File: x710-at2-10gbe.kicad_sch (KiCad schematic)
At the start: 18 parts, among them U1 EZX710AT2_S_LMR5

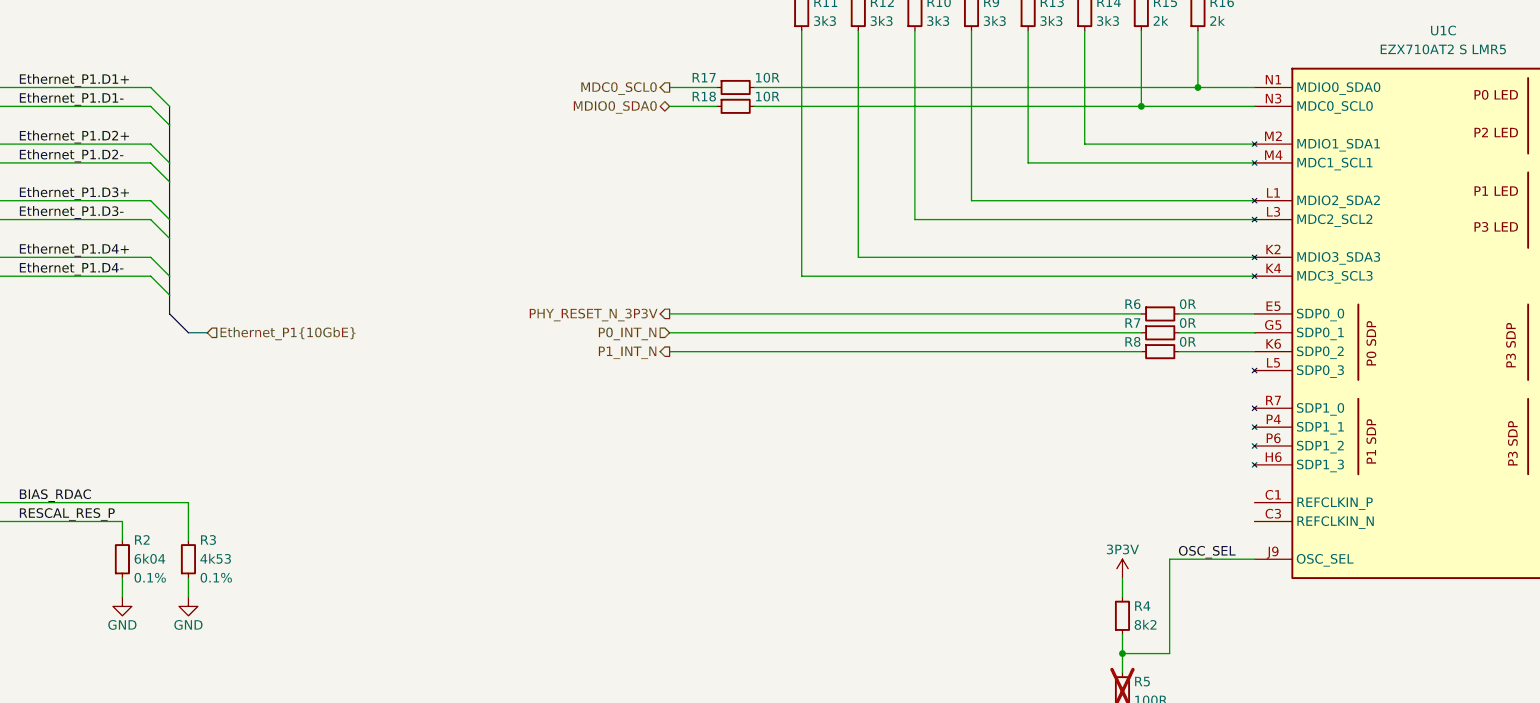
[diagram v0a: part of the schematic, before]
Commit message: [#80813] Add RJ45 connectors, add SMBus, FLASH SPI and misc
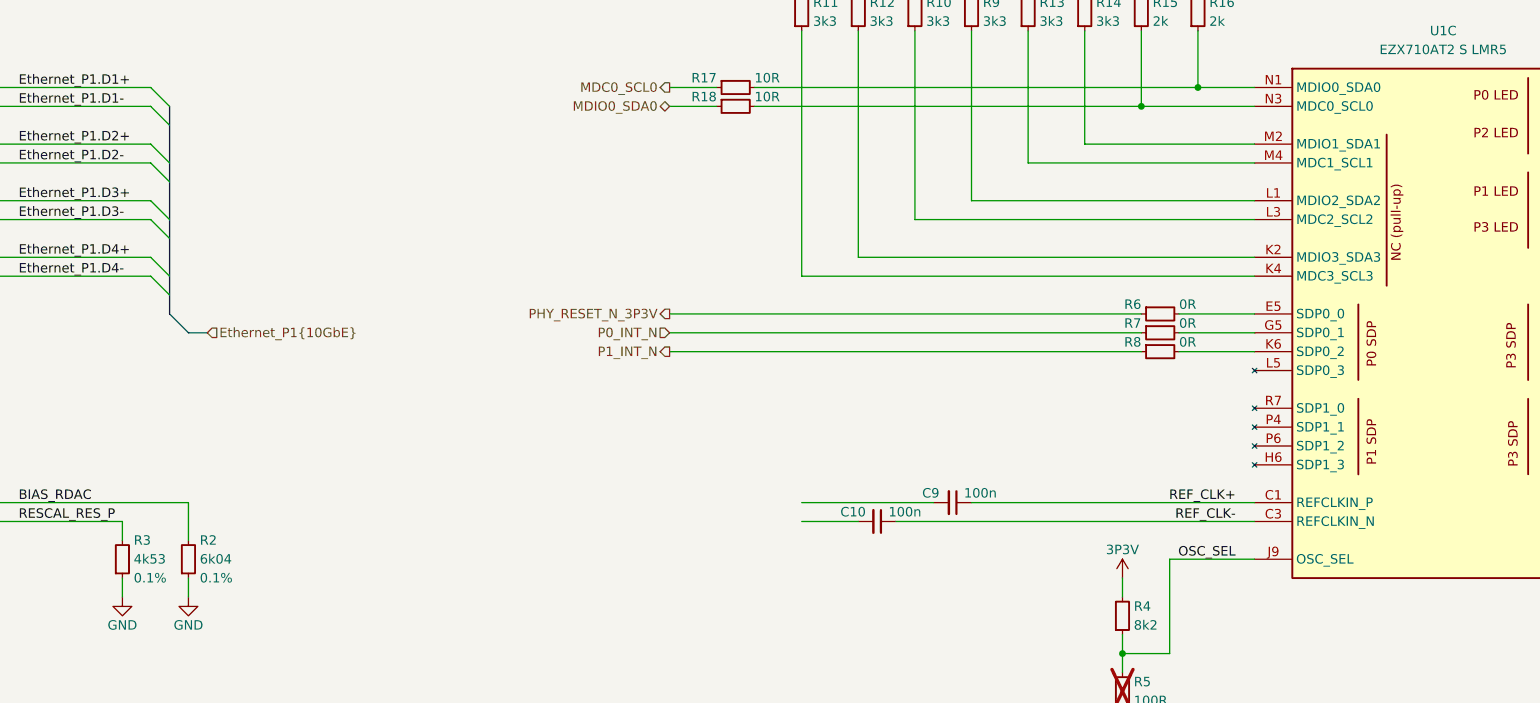
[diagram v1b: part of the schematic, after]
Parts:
- added C10, C9: C_100n_16V_X7R_0402, antmicro-footprints:C_0402_1005Metric, symbol antmicroCapacitors0402:C_100n_16V_X7R_0402
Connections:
- net BIAS_RDAC: now also R2.2; no longer R3.2
- net RESCAL_RES_P: now also R3.2; no longer R2.2
- net REF_CLK+: now reaches U1.C1 (REFCLKIN_P)
- net REF_CLK+: now also C9.1
- net REF_CLK-: now reaches U1.C3 (REFCLKIN_N)
- net REF_CLK-: now also C10.1
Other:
- moved on the sheet: R2, R3

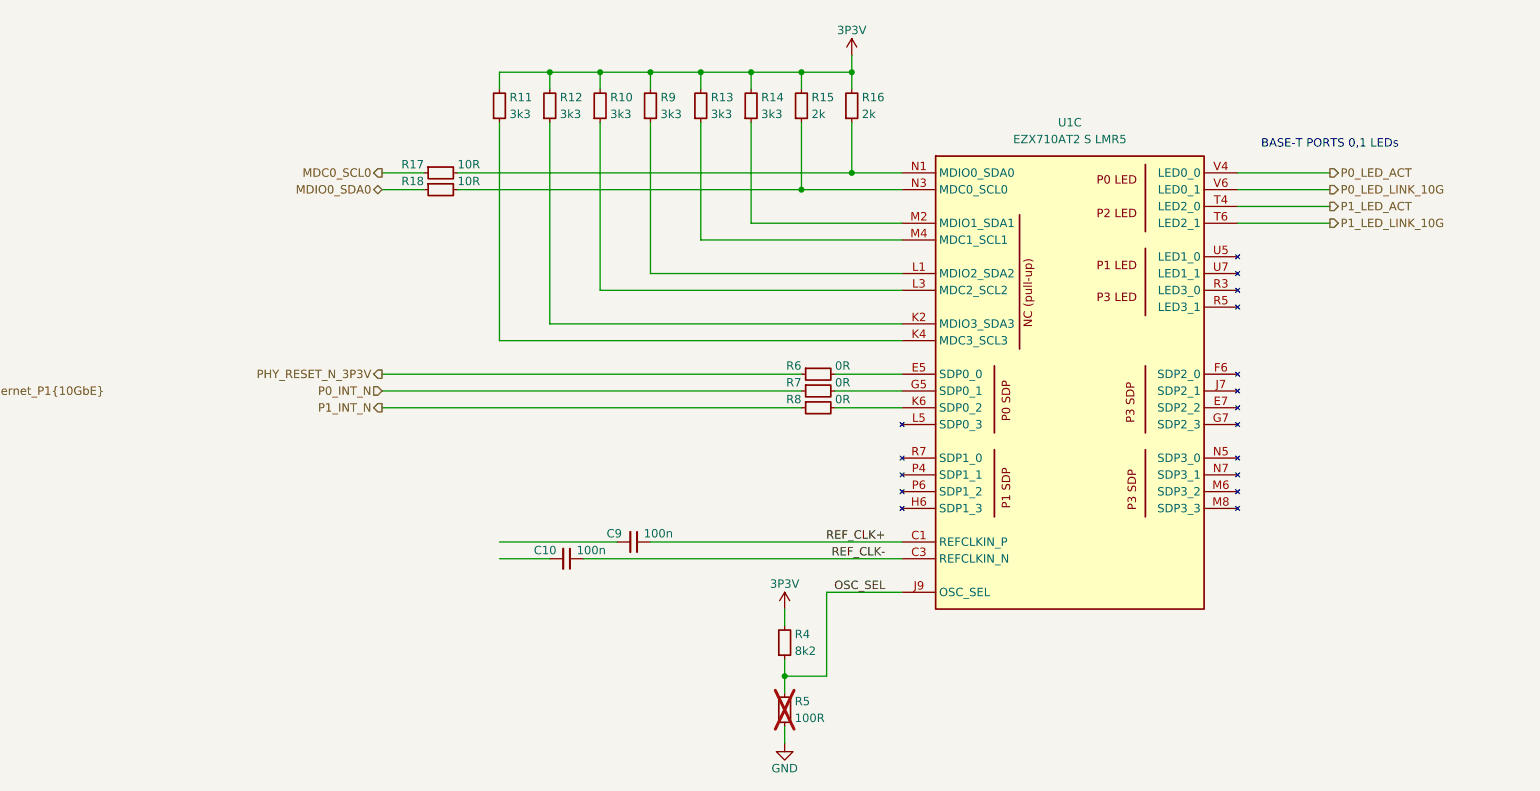
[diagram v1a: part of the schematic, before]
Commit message: [#80813] Add misc, improve schematic readability
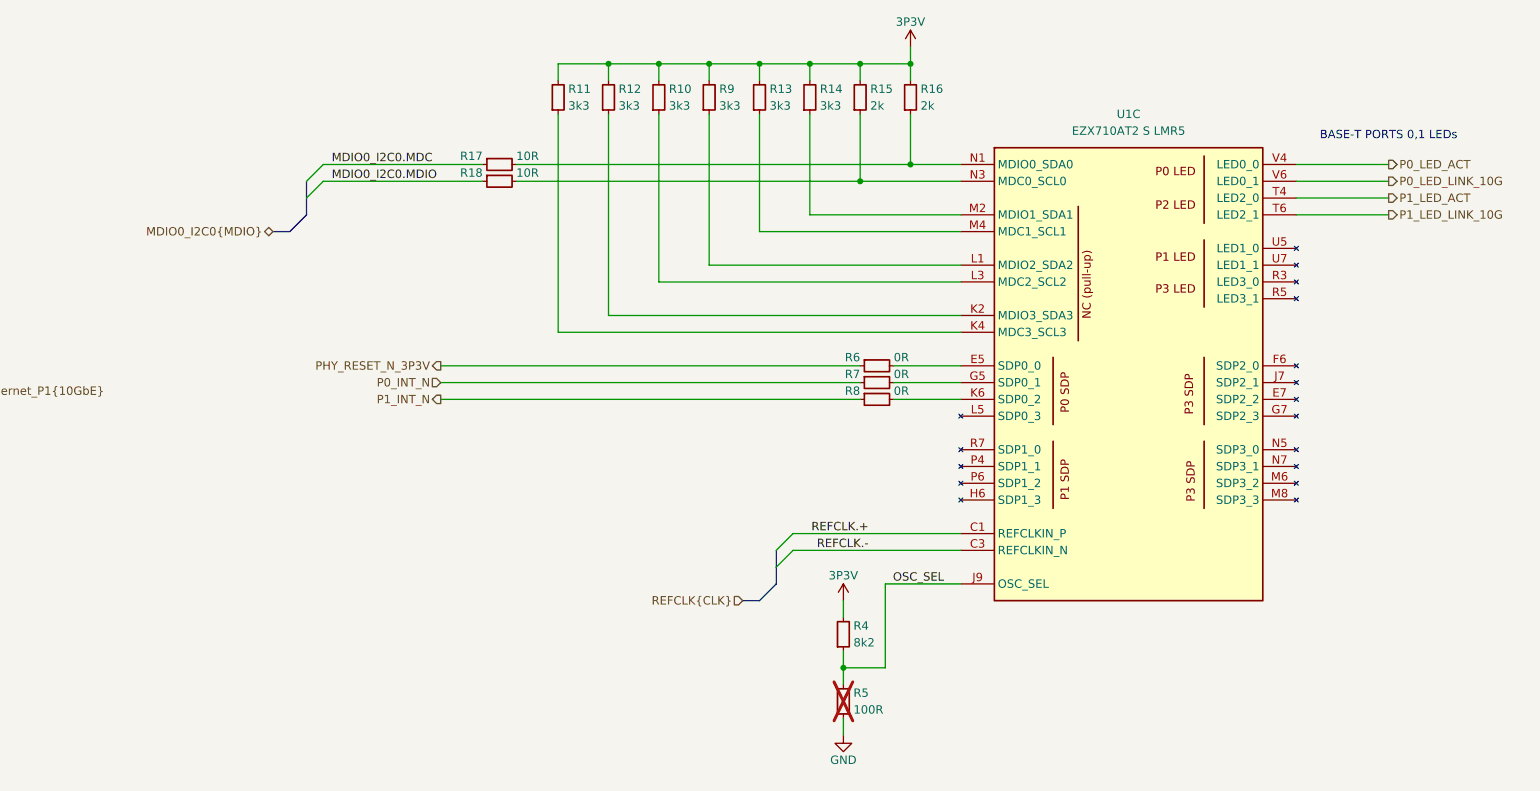
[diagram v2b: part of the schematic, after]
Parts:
- removed C10, C9: C_100n_16V_X7R_0402, antmicro-footprints:C_0402_1005Metric, symbol antmicroCapacitors0402:C_100n_16V_X7R_0402
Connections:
- net MDC0_SCL0 renamed MDIO0_I2C0.MDC
- net MDIO0_SDA0 renamed MDIO0_I2C0.MDIO
- net REF_CLK+ renamed REFCLK.+
- net REF_CLK- renamed REFCLK.-
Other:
- moved on the sheet: R10, R11, R12, R13, R14, R15, R16, R17, R18, R4, R5, R6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

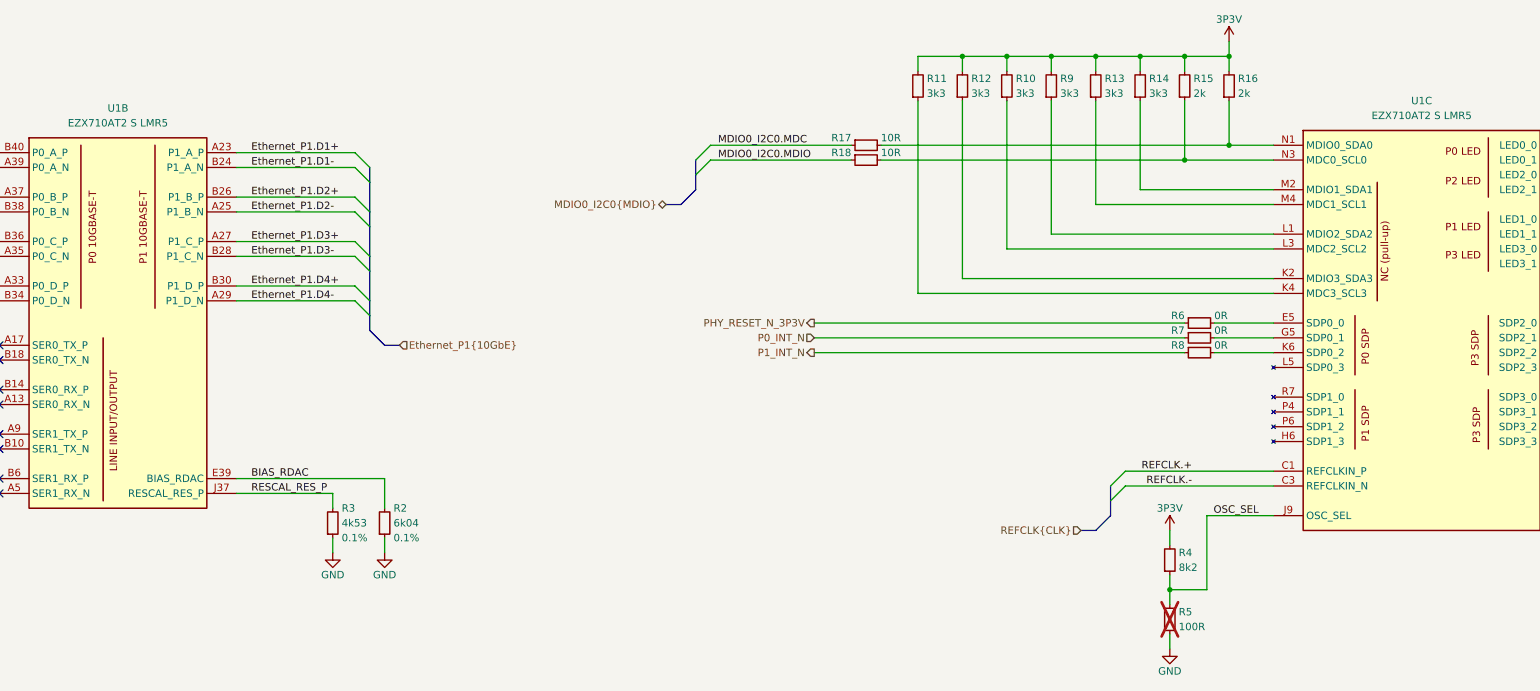
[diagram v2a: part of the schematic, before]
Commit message: [#80813] Change RJ45 connectors, reannotate schematics
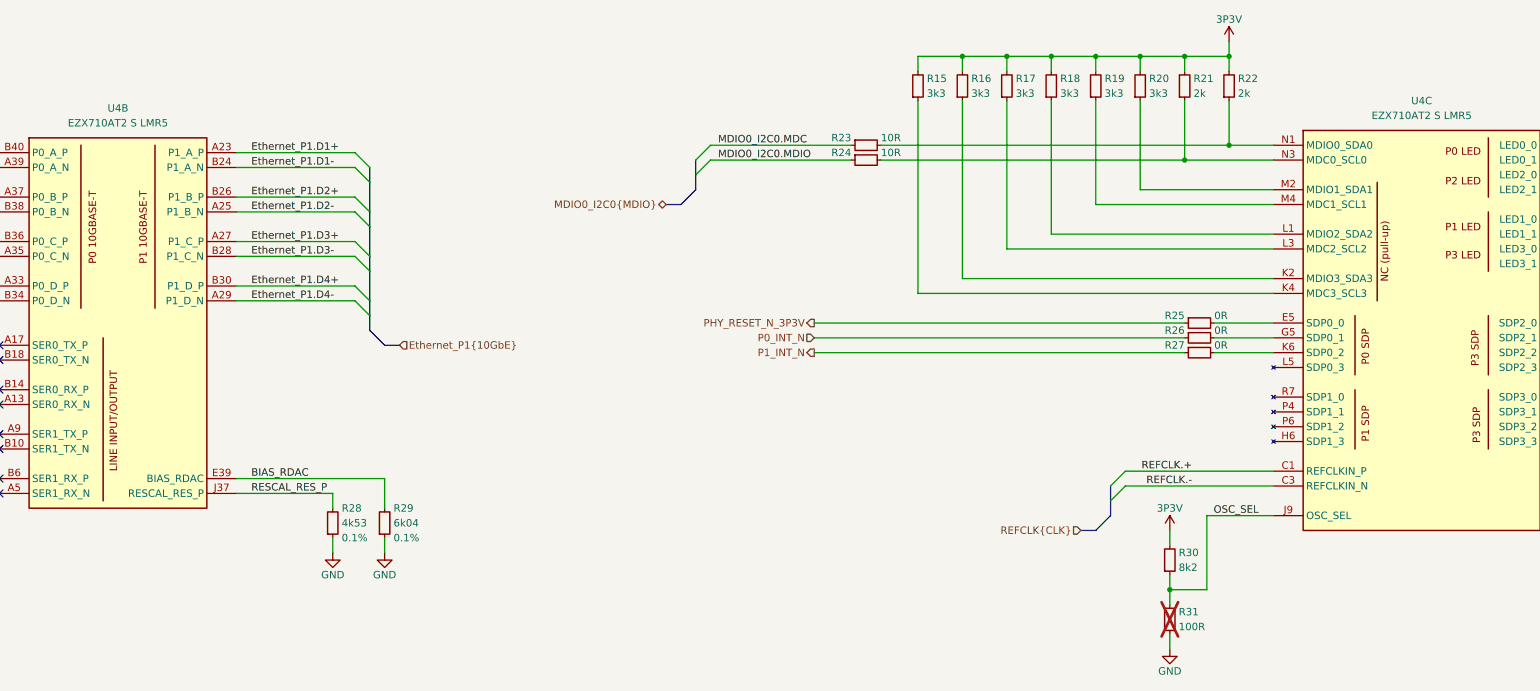
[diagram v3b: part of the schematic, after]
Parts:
- renumbered R11 to R15, R12 to R16, R10 to R17, R9 to R18, R13 to R19, R14 to R20, R15 to R21, R16 to R22, R17 to R23, R18 to R24, R6 to R25, R7 to R26, R8 to R27, R3 to R28, R2 to R29, R4 to R30, R5 to R31, U1 to U4
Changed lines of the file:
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@@
 		(on_board yes)
 		(dnp no)
-		(property "Reference" "#PWR02"
+		(property "Reference" "#PWR049"
 			(at 172.72 193.04 0)
 			(effects
@@
 			(project "10-gbe-expansion"
 				(path "/04bda987-e5eb-48b4-9e90-d8211dc11b39/46fcd652-659b-4e06-aa16-4947b5e55b68"
-					(reference "#PWR02")
+					(reference "#PWR049")
 					(unit 1)
 				)
@@
 		(on_board yes)
 		(dnp no)
-		(property "Reference" "R8"
+		(property "Reference" "R27"
 			(at 300.99 154.94 0)
 			(effects
@@
 			(project "10-gbe-expansion"
 				(path "/04bda987-e5eb-48b4-9e90-d8211dc11b39/46fcd652-659b-4e06-aa16-4947b5e55b68"
-					(reference "R8")
+					(reference "R27")
 					(unit 1)
 				)
@@
 		(on_board yes)
 		(dnp no)
-		(property "Reference" "R4"
+		(property "Reference" "R30"
 			(at 299.974 190.5 90)
 			(effects
@@
 			(project ""
 				(path "/04bda987-e5eb-48b4-9e90-d8211dc11b39/46fcd652-659b-4e06-aa16-4947b5e55b68"
-					(reference "R4")
+					(reference "R30")
 					(unit 1)
 				)
@@
 		(on_board yes)
 		(dnp no)
-		(property "Reference" "R13"
+		(property "Reference" "R19"
 			(at 287.274 109.22 90)
 			(effects
@@
 			(project "10-gbe-expansion"
 				(path "/04bda987-e5eb-48b4-9e90-d8211dc11b39/46fcd652-659b-4e06-aa16-4947b5e55b68"
-					(reference "R13")
+					(reference "R19")
 					(unit 1)
 				)
@@
 		(on_board yes)
 		(dnp no)
-		(property "Reference" "R7"
+		(property "Reference" "R26"
 			(at 300.99 152.4 0)
 			(effects
@@
 			(project "10-gbe-expansion"
 				(path "/04bda987-e5eb-48b4-9e90-d8211dc11b39/46fcd652-659b-4e06-aa16-4947b5e55b68"
-					(reference "R7")
+					(reference "R26")
 					(unit 1)
 				)
@@
 		(on_board yes)
 		(dnp no)
-		(property "Reference" "#PWR05"
+		(property "Reference" "#PWR046"
 			(at 308.61 106.68 0)
 			(effects
@@
 			(project "10-gbe-expansion"
 				(path "/04bda987-e5eb-48b4-9e90-d8211dc11b39/46fcd652-659b-4e06-aa16-4947b5e55b68"
-					(reference "#PWR05")
+					(reference "#PWR046")
 					(unit 1)
 				)
@@
 		(on_board yes)
 		(dnp no)
-		(property "Reference" "#PWR01"
+		(property "Reference" "#PWR048"
 			(at 163.83 193.04 0)
 			(effects
@@
 			(project ""
 				(path "/04bda987-e5eb-48b4-9e90-d8211dc11b39/46fcd652-659b-4e06-aa16-4947b5e55b68"
-					(reference "#PWR01")
+					(reference "#PWR048")
 					(unit 1)
 				)
@@
 		(on_board yes)
 		(dnp no)
-		(property "Reference" "R18"
+		(property "Reference" "R24"
 			(at 243.84 121.92 0)
 			(effects
@@
 			(project "10-gbe-expansion"
 				(path "/04bda987-e5eb-48b4-9e90-d8211dc11b39/46fcd652-659b-4e06-aa16-4947b5e55b68"
-					(reference "R18")
+					(reference "R24")
 					(unit 1)
 				)
@@
 		(on_board yes)
 		(dnp no)
-		(property "Reference" "#PWR03"
+		(property "Reference" "#PWR050"
 			(at 307.34 209.55 0)
 			(effects
@@
 			(project "10-gbe-expansion"
 				(path "/04bda987-e5eb-48b4-9e90-d8211dc11b39/46fcd652-659b-4e06-aa16-4947b5e55b68"
-					(reference "#PWR03")
+					(reference "#PWR050")
 					(unit 1)
 				)
@@
 		(on_board yes)
 		(dnp no)
-		(property "Reference" "R2"
+		(property "Reference" "R29"
 			(at 165.354 182.88 90)
 			(effects
@@
 			(project "10-gbe-expansion"
 				(path "/04bda987-e5eb-48b4-9e90-d8211dc11b39/46fcd652-659b-4e06-aa16-4947b5e55b68"
-					(reference "R2")
+					(reference "R29")
 					(unit 1)
 				)
@@
 		(dnp no)
 		(fields_autoplaced yes)
-		(property "Reference" "U1"
+		(property "Reference" "U4"
 			(at 118.11 114.3 0)
 			(effects
@@
 			(project ""
 				(path "/04bda987-e5eb-48b4-9e90-d8211dc11b39/46fcd652-659b-4e06-aa16-4947b5e55b68"
-					(reference "U1")
+					(reference "U4")
 					(unit 2)
 				)
@@
 		(on_board yes)
 		(dnp yes)
-		(property "Reference" "R5"
+		(property "Reference" "R31"
 			(at 299.974 200.66 90)
 			(effects
@@
 			(project ""
 				(path "/04bda987-e5eb-48b4-9e90-d8211dc11b39/46fcd652-659b-4e06-aa16-4947b5e55b68"
-					(reference "R5")
+					(reference "R31")
 					(unit 1)
 				)
@@
 		(on_board yes)
 		(dnp no)
-		(property "Reference" "R17"
+		(property "Reference" "R23"
 			(at 243.84 119.38 0)
 			(effects
@@
 			(project ""
 				(path "/04bda987-e5eb-48b4-9e90-d8211dc11b39/46fcd652-659b-4e06-aa16-4947b5e55b68"
-					(reference "R17")
+					(reference "R23")
 					(unit 1)
 				)
@@
 		(on_board yes)
 		(dnp no)
-		(property "Reference" "R9"
+		(property "Reference" "R18"
 			(at 279.654 109.22 90)
 			(effects
@@
 			(project ""
 				(path "/04bda987-e5eb-48b4-9e90-d8211dc11b39/46fcd652-659b-4e06-aa16-4947b5e55b68"
-					(reference "R9")
+					(reference "R18")
 					(unit 1)
 				)
@@
 		(on_board yes)
 		(dnp no)
-		(property "Reference" "R3"
+		(property "Reference" "R28"
 			(at 156.464 182.88 90)
 			(effects
@@
 			(project "10-gbe-expansion"
 				(path "/04bda987-e5eb-48b4-9e90-d8211dc11b39/46fcd652-659b-4e06-aa16-4947b5e55b68"
-					(reference "R3")
+					(reference "R28")
 					(unit 1)
 				)
@@
 		(dnp no)
 		(fields_autoplaced yes)
-		(property "Reference" "U1"
+		(property "Reference" "U4"
 			(at 341.63 113.03 0)
 			(effects
@@
 			(project ""
 				(path "/04bda987-e5eb-48b4-9e90-d8211dc11b39/46fcd652-659b-4e06-aa16-4947b5e55b68"
-					(reference "U1")
+					(reference "U4")
 					(unit 3)
 				)
@@
 		(on_board yes)
 		(dnp no)
-		(property "Reference" "R15"
+		(property "Reference" "R21"
 			(at 302.514 109.22 90)
 			(effects
@@
 			(project ""
 				(path "/04bda987-e5eb-48b4-9e90-d8211dc11b39/46fcd652-659b-4e06-aa16-4947b5e55b68"
-					(reference "R15")
+					(reference "R21")
 					(unit 1)
 				)
@@
 		(on_board yes)
 		(dnp no)
-		(property "Reference" "R16"
+		(property "Reference" "R22"
 			(at 310.134 109.22 90)
 			(effects
@@
 			(project "10-gbe-expansion"
 				(path "/04bda987-e5eb-48b4-9e90-d8211dc11b39/46fcd652-659b-4e06-aa16-4947b5e55b68"
-					(reference "R16")
+					(reference "R22")
 					(unit 1)
 				)
@@
 		(on_board yes)
 		(dnp no)
-		(property "Reference" "R10"
+		(property "Reference" "R17"
 			(at 272.034 109.22 90)
 			(effects
@@
 			(project "10-gbe-expansion"
 				(path "/04bda987-e5eb-48b4-9e90-d8211dc11b39/46fcd652-659b-4e06-aa16-4947b5e55b68"
-					(reference "R10")
+					(reference "R17")
 					(unit 1)
 				)
@@
 		(on_board yes)
 		(dnp no)
-		(property "Reference" "R12"
+		(property "Reference" "R16"
 			(at 264.414 109.22 90)
 			(effects
@@
 			(project "10-gbe-expansion"
 				(path "/04bda987-e5eb-48b4-9e90-d8211dc11b39/46fcd652-659b-4e06-aa16-4947b5e55b68"
-					(reference "R12")
+					(reference "R16")
 					(unit 1)
 				)
@@
 		(on_board yes)
 		(dnp no)
-		(property "Reference" "R11"
+		(property "Reference" "R15"
 			(at 256.794 109.22 90)
 			(effects
@@
 			(project "10-gbe-expansion"
 				(path "/04bda987-e5eb-48b4-9e90-d8211dc11b39/46fcd652-659b-4e06-aa16-4947b5e55b68"
-					(reference "R11")
+					(reference "R15")
 					(unit 1)
 				)
@@
 		(on_board yes)
 		(dnp no)
-		(property "Reference" "R14"
+		(property "Reference" "R20"
 			(at 294.894 109.22 90)
 			(effects
@@
 			(project "10-gbe-expansion"
 				(path "/04bda987-e5eb-48b4-9e90-d8211dc11b39/46fcd652-659b-4e06-aa16-4947b5e55b68"
-					(reference "R14")
+					(reference "R20")
 					(unit 1)
 				)
@@
 		(on_board yes)
 		(dnp no)
-		(property "Reference" "R6"
+		(property "Reference" "R25"
 			(at 300.99 149.86 0)
 			(effects
@@
 			(project ""
 				(path "/04bda987-e5eb-48b4-9e90-d8211dc11b39/46fcd652-659b-4e06-aa16-4947b5e55b68"
-					(reference "R6")
+					(reference "R25")
 					(unit 1)
 				)
@@
 		(on_board yes)
 		(dnp no)
-		(property "Reference" "#PWR04"
+		(property "Reference" "#PWR047"
 			(at 298.45 190.5 0)
 			(effects
@@
 			(project "10-gbe-expansion"
 				(path "/04bda987-e5eb-48b4-9e90-d8211dc11b39/46fcd652-659b-4e06-aa16-4947b5e55b68"
-					(reference "#PWR04")
+					(reference "#PWR047")
 					(unit 1)
 				)
